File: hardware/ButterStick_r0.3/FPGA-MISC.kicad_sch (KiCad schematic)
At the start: 1 part, among them U4 ECP5UM5G_85_CABGA381

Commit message: hw.r0d3: complete first pass of routing
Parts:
- added C23: 100nF, Capacitor_SMD:C_0402_1005Metric, symbol Device:C
- added C24: 10nF, Capacitor_SMD:C_0402_1005Metric, symbol Device:C
- added R54: 20R, Resistor_SMD:R_0402_1005Metric, symbol Device:R
- added X1: ASDMB, gkl_time:Oscilator_2.5x2.0, symbol gkl_time:TYETBCSANF-32.000000
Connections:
- net LEDC0 is gone; now on net I2C0.SCL: U4.E14 (PT85B)
- net LEDC2 is gone; now on net LED5: U4.E13 (PT80B)
- net PDM2 is gone; now on net LED0: U4.C13 (PT78B)
- net +3V3: now also X1.1 (NC), X1.4 (VDD)
- net CLK_IN: now also R54.2
- net ETH0.TX1: now also U4.E15 (PT107B); no longer U4.A18 (PT119A)
- net ETH0.TX_CLK: now also U4.A18 (PT119A); no longer U4.E15 (PT107B)
- net I2C0.SCL: no longer U4.A14 (PT83A)
- net LED1: now also U4.D12 (PT74A/GR_PCLK1_0)
- net LED4: now also U4.D13 (PT80A)
- net LED5: no longer U4.B15 (PT105A)
- net ULIP_VDDIO: no longer U4.F10 (VCCIO0[2]), U4.F9 (VCCIO0[2])
- net USB0.DATA4: now also U4.C6 (PT11A); no longer U4.A9 (PT60A/GR_PCLK0_1)
- net USB0.RESET: now also U4.C9 (PT54A); no longer U4.C6 (PT11A)
- net VDDIO_EN: now also U4.E12 (PT74B/GR_PCLK1_1); no longer U4.D12 (PT74A/GR_PCLK1_0)
- net SYZYGY2.C2P_CLK_N: now reaches U4.B10 (PT60B/GR_PCLK0_0)
- net SYZYGY2.S9: now reaches U4.D10 (PT56A)
- net SYZYGY2.S8: now reaches U4.E10 (PT56B)
- net SDMMC0.DAT1: now reaches U4.A12 (PT76A)
- net SDMMC0.CMD: now reaches U4.A13 (PT76B)
- net SDMMC0.CK: now reaches U4.B13 (PT78A)
- net LEDC1 renamed SDMMC0.CD
- net PDM0 renamed SDMMC0.DAT0
- net S0 renamed SYZYGY2.S0
- net S1 renamed SYZYGY2.S1
- net S2 renamed SYZYGY2.S2
- net S3 renamed SYZYGY2.S3
- net S4 renamed SYZYGY2.S4
- net S5 renamed SYZYGY2.S5
- net S6 renamed SYZYGY2.P2C_CLK_P
- net S7 renamed SYZYGY2.S7
- net S8 renamed SYZYGY2.P2C_CLK_N
- net S9 renamed SYZYGY2.S6
- new net: R54.1, X1.3 (OUT)
- new net GND: C23.2, C24.2, X1.2 (GND)
- new net SDMMC0.DAT2: U4.B15 (PT105A)
- new net SDMMC0.DAT3: U4.A14 (PT83A)
- new net SYZYGY2.C2P_CLK_P: U4.A9 (PT60A/GR_PCLK0_1)
- new net VIO1: C23.1, C24.1, U4.F10 (VCCIO0[2]), U4.F9 (VCCIO0[2])
- no-connect marks 1 -> 0

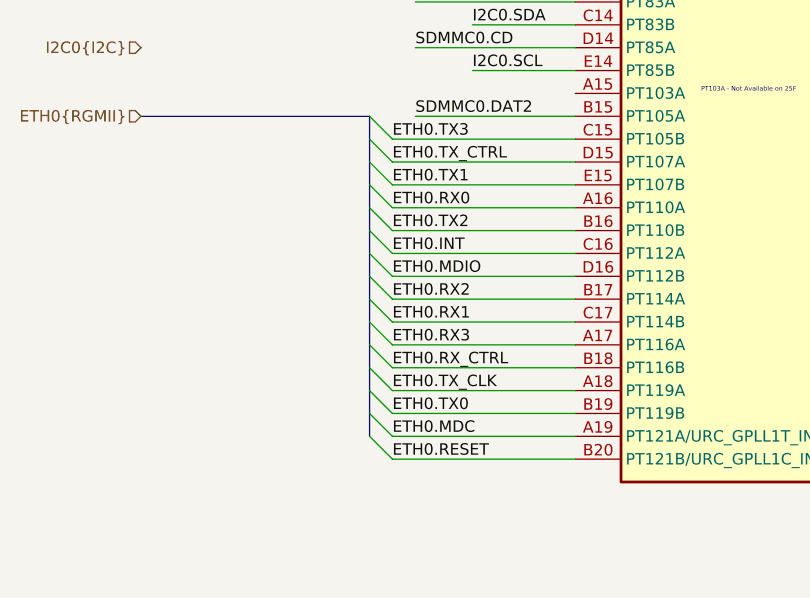
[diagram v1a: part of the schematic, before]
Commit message: hw.r0d3: Updated all DCDC supplies Added serdes power supplies
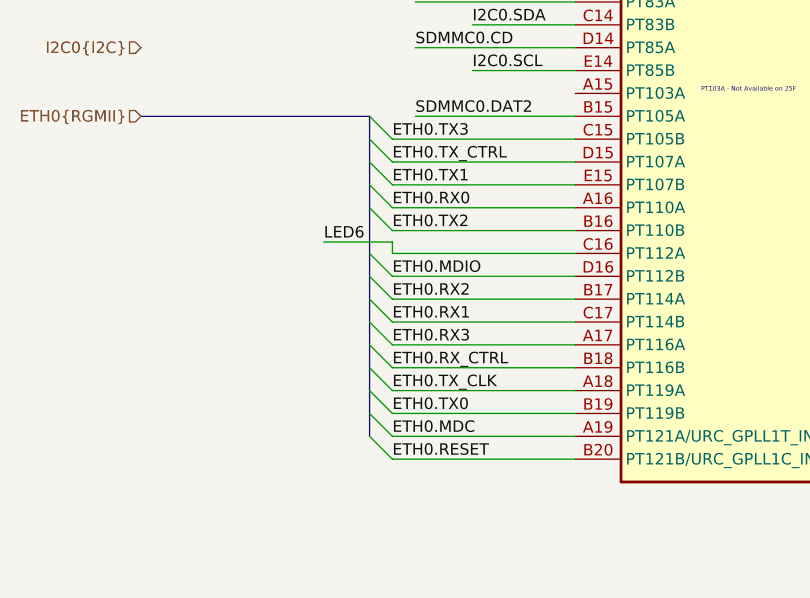
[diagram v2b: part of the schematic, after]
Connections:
- net ETH0.INT renamed LED6
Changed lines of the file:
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@@
-(kicad_sch (version 20200618) (host eeschema "5.99.0-unknown-476558e~101~ubuntu18.04.1")
+(kicad_sch (version 20200618) (host eeschema "5.99.0-unknown-73168a9~101~ubuntu18.04.1")
   (page 6 19)
   (paper "A4")
@@
     (stroke (width 0.1524) (type solid) (color 0 0 0 0))
   )
-  (bus_entry (at 57.15 125.73) (size -2.54 -2.54)
-    (stroke (width 0.1524) (type solid) (color 0 0 0 0))
-  )
   (bus_entry (at 57.15 128.27) (size -2.54 -2.54)
     (stroke (width 0.1524) (type solid) (color 0 0 0 0))
@@
     (stroke (width 0) (type solid) (color 0 0 0 0))
   )
+  (wire (pts (xy 49.53 124.46) (xy 57.15 124.46))
+    (stroke (width 0) (type solid) (color 0 0 0 0))
+  )
   (wire (pts (xy 53.34 44.45) (xy 62.23 44.45))
     (stroke (width 0) (type solid) (color 0 0 0 0))
@@
     (stroke (width 0) (type solid) (color 0 0 0 0))
   )
+  (wire (pts (xy 57.15 125.73) (xy 57.15 124.46))
+    (stroke (width 0) (type solid) (color 0 0 0 0))
+  )
   (wire (pts (xy 57.15 125.73) (xy 77.47 125.73))
     (stroke (width 0) (type solid) (color 0 0 0 0))
@@
     (stroke (width 0) (type solid) (color 0 0 0 0))
   )
-  (bus (pts (xy 54.61 115.57) (xy 54.61 118.11))
-    (stroke (width 0) (type solid) (color 0 0 0 0))
-  )
-  (bus (pts (xy 54.61 118.11) (xy 54.61 123.19))
-    (stroke (width 0) (type solid) (color 0 0 0 0))
-  )
-  (bus (pts (xy 54.61 123.19) (xy 54.61 128.27))
-    (stroke (width 0) (type solid) (color 0 0 0 0))
-  )
-  (bus (pts (xy 54.61 128.27) (xy 54.61 133.35))
-    (stroke (width 0) (type solid) (color 0 0 0 0))
-  )
-  (bus (pts (xy 54.61 133.35) (xy 54.61 138.43))
-    (stroke (width 0) (type solid) (color 0 0 0 0))
-  )
-  (bus (pts (xy 54.61 138.43) (xy 54.61 143.51))
-    (stroke (width 0) (type solid) (color 0 0 0 0))
-  )
-  (bus (pts (xy 54.61 143.51) (xy 54.61 146.05))
+  (bus (pts (xy 54.61 115.57) (xy 54.61 120.65))
+    (stroke (width 0) (type solid) (color 0 0 0 0))
+  )
+  (bus (pts (xy 54.61 120.65) (xy 54.61 125.73))
+    (stroke (width 0) (type solid) (color 0 0 0 0))
+  )
+  (bus (pts (xy 54.61 125.73) (xy 54.61 130.81))
+    (stroke (width 0) (type solid) (color 0 0 0 0))
+  )
+  (bus (pts (xy 54.61 130.81) (xy 54.61 135.89))
+    (stroke (width 0) (type solid) (color 0 0 0 0))
+  )
+  (bus (pts (xy 54.61 135.89) (xy 54.61 140.97))
+    (stroke (width 0) (type solid) (color 0 0 0 0))
+  )
+  (bus (pts (xy 54.61 140.97) (xy 54.61 146.05))
     (stroke (width 0) (type solid) (color 0 0 0 0))
   )
@@
     (effects (font (size 1.27 1.27)) (justify right bottom))
   )
+  (label "LED6" (at 49.53 124.46 0)
+    (effects (font (size 1.27 1.27)) (justify left bottom))
+  )
   (label "ETH0.RX_CLK" (at 57.15 67.31 0)
     (effects (font (size 1.27 1.27)) (justify left bottom))
@@
     (effects (font (size 1.27 1.27)) (justify left bottom))
   )
-  (label "ETH0.INT" (at 57.15 125.73 0)
-    (effects (font (size 1.27 1.27)) (justify left bottom))
-  )

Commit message: hw.r0d3: Tweaking routing
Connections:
- net ETH0.TX0: now also U4.C15 (PT105B); no longer U4.B19 (PT119B)
- net ETH0.TX1: now also U4.B16 (PT110B); no longer U4.E15 (PT107B)
- net ETH0.TX2: now also U4.A18 (PT119A); no longer U4.B16 (PT110B)
- net ETH0.TX3: now also U4.B19 (PT119B); no longer U4.C15 (PT105B)
- net ETH0.TX_CLK: now also U4.E15 (PT107B); no longer U4.A18 (PT119A)
- net SDMMC0.CD: now also U4.B15 (PT105A); no longer U4.D14 (PT85A)
- net SDMMC0.DAT2: now also U4.D14 (PT85A); no longer U4.B15 (PT105A)
- net USB0.DATA0: now also U4.B9 (PT58A); no longer U4.C8 (PT15A)
- net USB0.DATA1: now also U4.C6 (PT11A); no longer U4.B8 (PT15B)
- net USB0.DATA2: now also U4.A7 (PT18A); no longer U4.B9 (PT58A)
- net USB0.DATA3: now also U4.E9 (PT20B); no longer U4.C10 (PT58B)
- net USB0.DATA4: now also U4.A8 (PT18B); no longer U4.C6 (PT11A)
- net USB0.DATA5: now also U4.D9 (PT20A); no longer U4.E9 (PT20B)
- net USB0.DATA6: now also U4.C10 (PT58B); no longer U4.A8 (PT18B)
- net USB0.DIR: now also U4.A6 (PT4A/ULC_GPLL1T_IN); no longer U4.B6 (PT4B/ULC_GPLL1C_IN)
- net USB0.NXT: now also U4.B8 (PT15B); no longer U4.D9 (PT20A)
- net USB0.REFCLK: now also U4.B6 (PT4B/ULC_GPLL1C_IN); no longer U4.A6 (PT4A/ULC_GPLL1T_IN)
- net USB0.STP: now also U4.C8 (PT15A); no longer U4.A7 (PT18A)
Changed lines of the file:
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@@
-    (stroke (width 0) (type solid) (color 0 0 0 0))
-  )
-  (wire (pts (xy 49.53 124.46) (xy 57.15 124.46))
     (stroke (width 0) (type solid) (color 0 0 0 0))
   )
@@
     (stroke (width 0) (type solid) (color 0 0 0 0))
   )
-  (wire (pts (xy 57.15 125.73) (xy 57.15 124.46))
-    (stroke (width 0) (type solid) (color 0 0 0 0))
-  )
-  (wire (pts (xy 57.15 125.73) (xy 77.47 125.73))
-    (stroke (width 0) (type solid) (color 0 0 0 0))
-  )
   (wire (pts (xy 57.15 128.27) (xy 77.47 128.27))
     (stroke (width 0) (type solid) (color 0 0 0 0))
@@
     (stroke (width 0) (type solid) (color 0 0 0 0))
   )
+  (wire (pts (xy 62.23 125.73) (xy 77.47 125.73))
+    (stroke (width 0) (type solid) (color 0 0 0 0))
+  )
   (wire (pts (xy 63.5 80.01) (xy 77.47 80.01))
     (stroke (width 0) (type solid) (color 0 0 0 0))
@@
     (stroke (width 0) (type solid) (color 0 0 0 0))
   )
-  (bus (pts (xy 54.61 120.65) (xy 54.61 125.73))
-    (stroke (width 0) (type solid) (color 0 0 0 0))
-  )
-  (bus (pts (xy 54.61 125.73) (xy 54.61 130.81))
-    (stroke (width 0) (type solid) (color 0 0 0 0))
-  )
-  (bus (pts (xy 54.61 130.81) (xy 54.61 135.89))
-    (stroke (width 0) (type solid) (color 0 0 0 0))
-  )
-  (bus (pts (xy 54.61 135.89) (xy 54.61 140.97))
-    (stroke (width 0) (type solid) (color 0 0 0 0))
-  )
-  (bus (pts (xy 54.61 140.97) (xy 54.61 146.05))
+  (bus (pts (xy 54.61 120.65) (xy 54.61 128.27))
+    (stroke (width 0) (type solid) (color 0 0 0 0))
+  )
+  (bus (pts (xy 54.61 128.27) (xy 54.61 133.35))
+    (stroke (width 0) (type solid) (color 0 0 0 0))
+  )
+  (bus (pts (xy 54.61 133.35) (xy 54.61 138.43))
+    (stroke (width 0) (type solid) (color 0 0 0 0))
+  )
+  (bus (pts (xy 54.61 138.43) (xy 54.61 143.51))
+    (stroke (width 0) (type solid) (color 0 0 0 0))
+  )
+  (bus (pts (xy 54.61 143.51) (xy 54.61 146.05))
     (stroke (width 0) (type solid) (color 0 0 0 0))
   )
@@
     (effects (font (size 1.27 1.27)) (justify right bottom))
   )
-  (label "LED6" (at 49.53 124.46 0)
-    (effects (font (size 1.27 1.27)) (justify left bottom))
-  )
   (label "ETH0.RX_CLK" (at 57.15 67.31 0)
     (effects (font (size 1.27 1.27)) (justify left bottom))
   )
-  (label "ETH0.TX3" (at 57.15 113.03 0)
+  (label "ETH0.TX0" (at 57.15 113.03 0)
     (effects (font (size 1.27 1.27)) (justify left bottom))
   )
@@
     (effects (font (size 1.27 1.27)) (justify left bottom))
   )
-  (label "ETH0.TX1" (at 57.15 118.11 0)
+  (label "ETH0.TX_CLK" (at 57.15 118.11 0)
     (effects (font (size 1.27 1.27)) (justify left bottom))
   )
@@
     (effects (font (size 1.27 1.27)) (justify left bottom))
   )
-  (label "ETH0.TX2" (at 57.15 123.19 0)
+  (label "ETH0.TX1" (at 57.15 123.19 0)
     (effects (font (size 1.27 1.27)) (justify left bottom))
   )
@@
     (effects (font (size 1.27 1.27)) (justify left bottom))
   )
-  (label "ETH0.TX_CLK" (at 57.15 140.97 0)
-    (effects (font (size 1.27 1.27)) (justify left bottom))
-  )
-  (label "ETH0.TX0" (at 57.15 143.51 0)
+  (label "ETH0.TX2" (at 57.15 140.97 0)
+    (effects (font (size 1.27 1.27)) (justify left bottom))
+  )
+  (label "ETH0.TX3" (at 57.15 143.51 0)
     (effects (font (size 1.27 1.27)) (justify left bottom))
   )
@@
     (effects (font (size 1.27 1.27)) (justify left bottom))
   )
-  (label "SDMMC0.CD" (at 59.69 102.87 0)
-    (effects (font (size 1.27 1.27)) (justify left bottom))
-  )
-  (label "SDMMC0.DAT2" (at 59.69 110.49 0)
+  (label "SDMMC0.DAT2" (at 59.69 102.87 0)
+    (effects (font (size 1.27 1.27)) (justify left bottom))
+  )
+  (label "SDMMC0.CD" (at 59.69 110.49 0)
+    (effects (font (size 1.27 1.27)) (justify left bottom))
+  )
+  (label "LED6" (at 62.23 125.73 0)
     (effects (font (size 1.27 1.27)) (justify left bottom))
   )
@@
     (effects (font (size 1.27 1.27)) (justify left bottom))
   )
-  (label "USB0.REFCLK" (at 198.12 82.55 0)
-    (effects (font (size 1.27 1.27)) (justify left bottom))
-  )
-  (label "USB0.DIR" (at 198.12 85.09 0)
-    (effects (font (size 1.27 1.27)) (justify left bottom))
-  )
-  (label "USB0.DATA4" (at 198.12 97.79 0)
+  (label "USB0.DIR" (at 198.12 82.55 0)
+    (effects (font (size 1.27 1.27)) (justify left bottom))
+  )
+  (label "USB0.REFCLK" (at 198.12 85.09 0)
+    (effects (font (size 1.27 1.27)) (justify left bottom))
+  )
+  (label "USB0.DATA1" (at 198.12 97.79 0)
     (effects (font (size 1.27 1.27)) (justify left bottom))
   )
@@
     (effects (font (size 1.27 1.27)) (justify left bottom))
   )
-  (label "USB0.DATA0" (at 198.12 107.95 0)
-    (effects (font (size 1.27 1.27)) (justify left bottom))
-  )
-  (label "USB0.DATA1" (at 198.12 110.49 0)
-    (effects (font (size 1.27 1.27)) (justify left bottom))
-  )
-  (label "USB0.STP" (at 198.12 113.03 0)
-    (effects (font (size 1.27 1.27)) (justify left bottom))
-  )
-  (label "USB0.DATA6" (at 198.12 115.57 0)
-    (effects (font (size 1.27 1.27)) (justify left bottom))
-  )
-  (label "USB0.NXT" (at 198.12 118.11 0)
-    (effects (font (size 1.27 1.27)) (justify left bottom))
-  )
-  (label "USB0.DATA5" (at 198.12 120.65 0)
-    (effects (font (size 1.27 1.27)) (justify left bottom))
-  )
-  (label "USB0.DATA2" (at 198.12 130.81 0)
-    (effects (font (size 1.27 1.27)) (justify left bottom))
-  )
-  (label "USB0.DATA3" (at 198.12 133.35 0)
-    (effects (font (size 1.27 1.27)) (justify left bottom))
-  )
+  (label "USB0.STP" (at 198.12 107.95 0)
+    (effects (font (size 1.27 1.27)) (justify left bottom))
+  )
+  (label "USB0.NXT" (at 198.12 110.49 0)
+    (effects (font (size 1.27 1.27)) (justify left bottom))
+  )
+  (label "USB0.DATA2" (at 198.12 113.03 0)
+    (effects (font (size 1.27 1.27)) (justify left bottom))
+  )
+  (label "USB0.DATA4" (at 198.12 115.57 0)
+    (effects (font (size 1.27 1.27)) (justify left bottom))
+  )
+  (label "USB0.DATA5" (at 198.12 118.11 0)
+    (effects (font (size 1.27 1.27)) (justify left bottom))
+  )
+  (label "USB0.DATA3" (at 198.12 120.65 0)
+    (effects (font (size 1.27 1.27)) (justify left bottom))
+  )
+  (label "USB0.DATA0" (at 198.12 130.81 0)
+    (effects (font (size 1.27 1.27)) (justify left bottom))
+  )
+  (label "USB0.DATA6" (at 198.12 133.35 0)
+    (effects (font (size 1.27 1.27)) (justify left bottom))
+  )

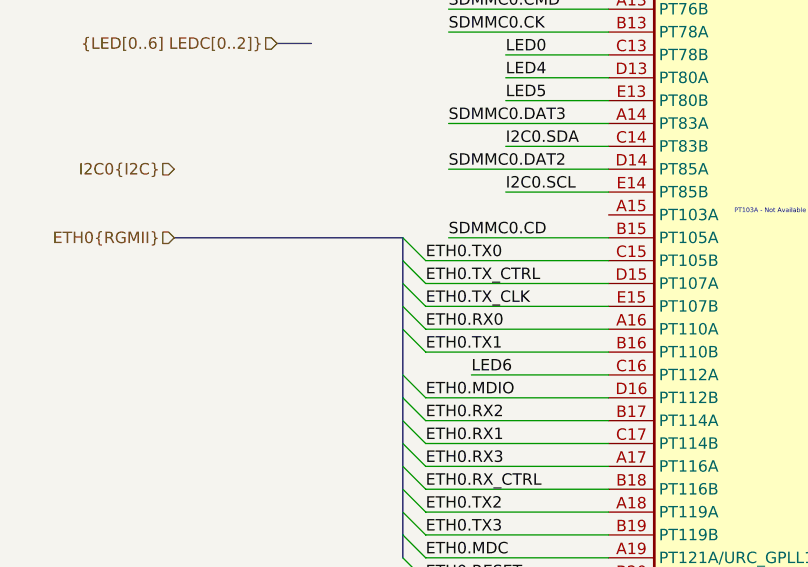
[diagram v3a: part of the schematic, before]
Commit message: hw.r0d3: Small routing tweaks
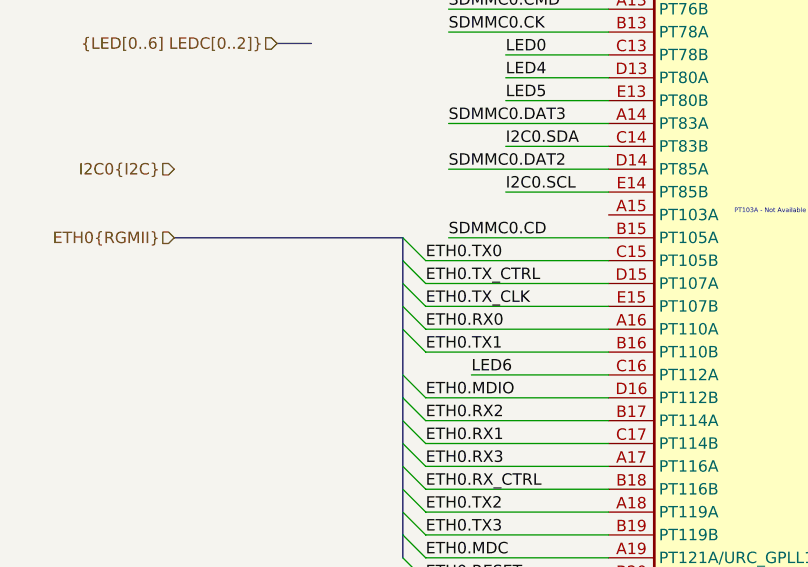
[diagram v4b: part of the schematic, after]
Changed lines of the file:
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@@
 (kicad_sch (version 20200618) (host eeschema "5.99.0-unknown-73168a9~101~ubuntu18.04.1")
-  (page 6 19)
+  (page 1 18)
   (paper "A4")
   (junction (at 261.62 78.74) (diameter 0) (color 0 0 0 0))
@@
     (stroke (width 0) (type solid) (color 0 0 0 0))
   )
-  (bus (pts (xy 54.61 110.49) (xy 54.61 115.57))
-    (stroke (width 0) (type solid) (color 0 0 0 0))
-  )
-  (bus (pts (xy 54.61 115.57) (xy 54.61 120.65))
-    (stroke (width 0) (type solid) (color 0 0 0 0))
-  )
+  (bus (pts (xy 54.61 110.49) (xy 54.61 113.03))
+    (stroke (width 0) (type solid) (color 0 0 0 0))
+  )
+  (bus (pts (xy 54.61 113.03) (xy 54.61 118.11))
+    (stroke (width 0) (type solid) (color 0 0 0 0))
+  )
+  (bus (pts (xy 54.61 118.11) (xy 54.61 120.65))
+    (stroke (width 0) (type solid) (color 0 0 0 0))
+  )
